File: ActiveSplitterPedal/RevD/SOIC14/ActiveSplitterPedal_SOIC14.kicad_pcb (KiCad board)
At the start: 2 copper layers, 112.5 x 86.4 mm, 97 parts, among them J1 MonoJack2Switch, J2 Barrel_Jack, J3 MonoJack2Switch, J4 MonoJack2Switch, J5 MonoJack2Switch, J6 MonoJack2Switch, U1 AP7370-50SA-7, U11 TL072, U12 TL074, U14 ISA0505, U15 MCP1754S-3302xCB, U16 TC593002ECB, U2 TL072, U3 TL074, U5 TL072, U6 TL074, U8 TL072, U9 TL074

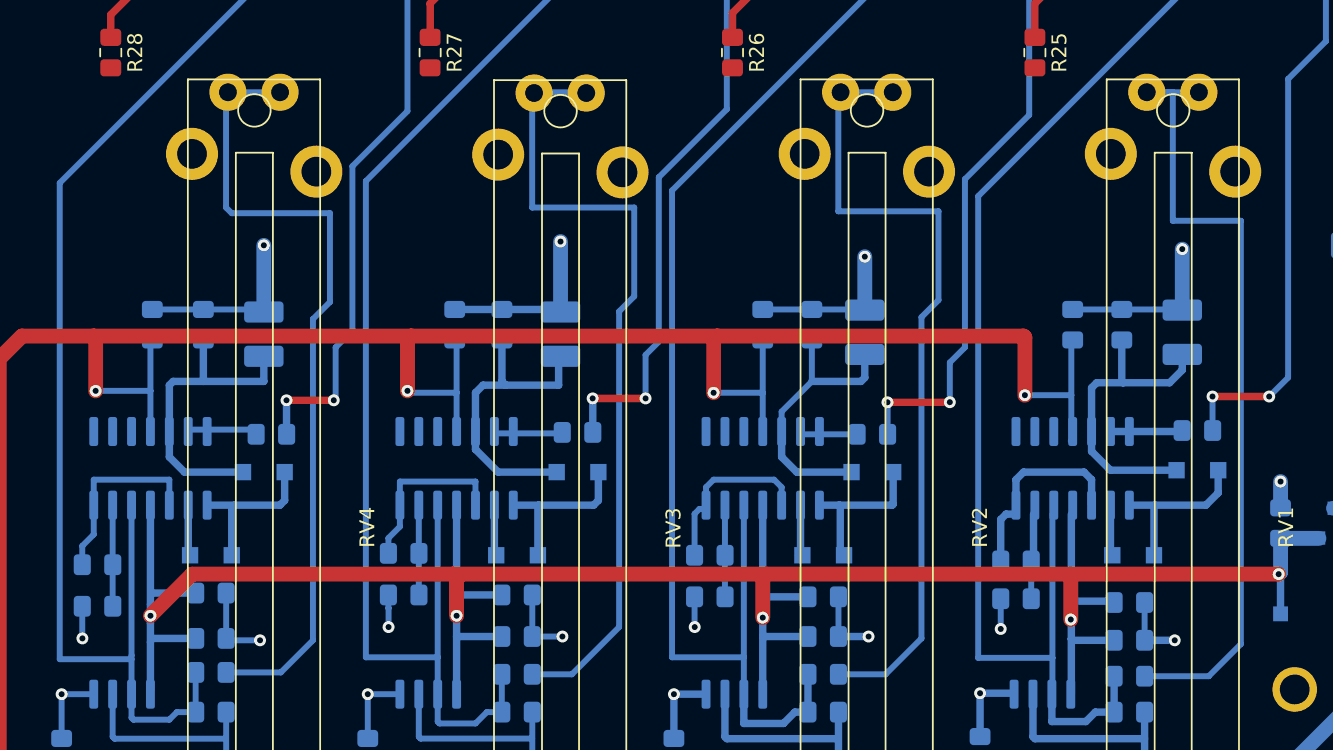
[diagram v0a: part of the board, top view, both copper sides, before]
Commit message: updated hw
added feedback cap to peak detector (help prevent oscillation)
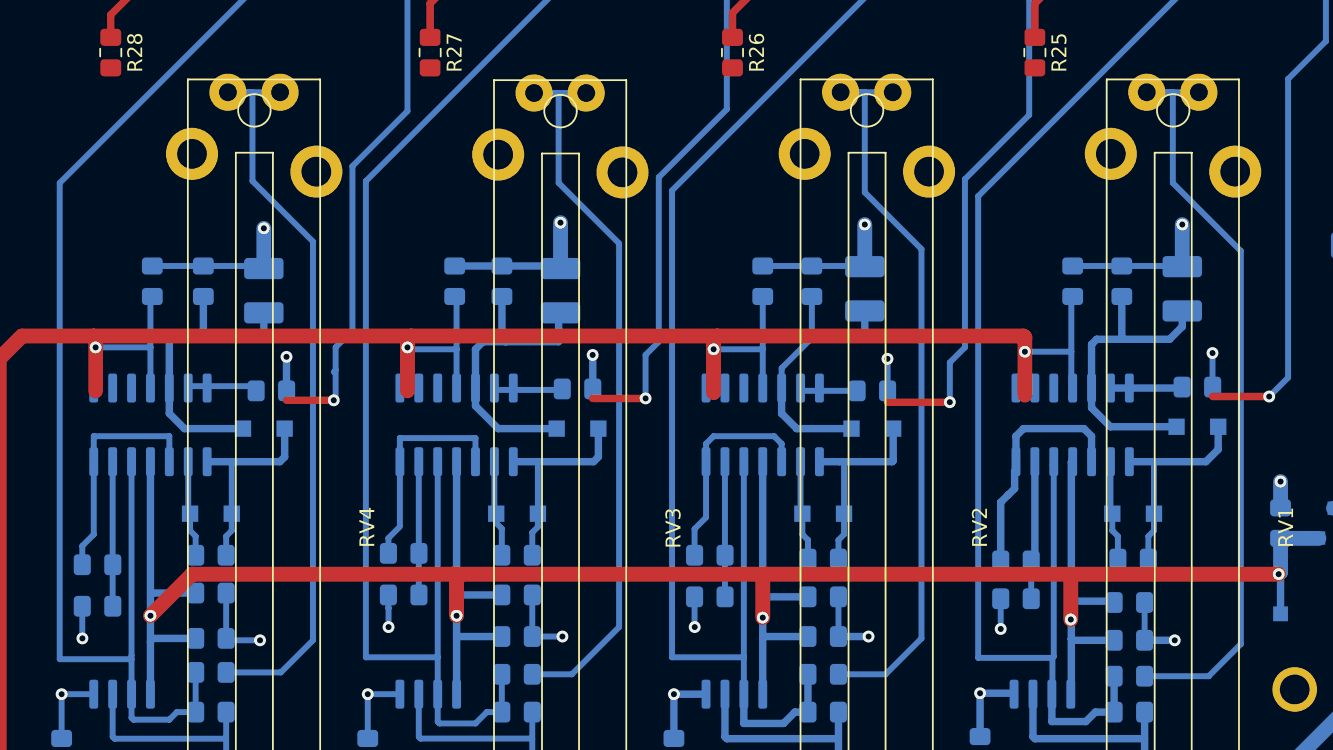
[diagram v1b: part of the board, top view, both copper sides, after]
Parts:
- added C10: 1nF, Capacitor_SMD:C_0805_2012Metric_Pad1.15x1.40mm_HandSolder, B.Cu at (102.4, 100.6)
- added C7: 1nF, Capacitor_SMD:C_0805_2012Metric_Pad1.15x1.40mm_HandSolder, B.Cu at (164.3, 100.8)
- added C8: 1nF, Capacitor_SMD:C_0805_2012Metric_Pad1.15x1.40mm_HandSolder, B.Cu at (143.5, 100.8)
- added C9: 1nF, Capacitor_SMD:C_0805_2012Metric_Pad1.15x1.40mm_HandSolder, B.Cu at (122.9, 100.6)
- moved C16 2.92 mm to (139.4, 82.2)
- moved C27 2.92 mm to (118.7, 82.2)
- moved C38 2.92 mm to (98.4, 82.2)
- moved C5 2.92 mm to (160.3, 82.2)
- moved D1 2.92 mm to (168.7, 91.9)
- moved R10 2.92 mm to (142.7, 82.2)
- moved R16 2.92 mm to (121.9, 82.2)
- moved R21 2.92 mm to (106.4, 89.5)
- moved R22 2.92 mm to (101.9, 82.2)
- moved R4 2.92 mm to (163.6, 82.2)
- moved R9 2.92 mm to (146.8, 89.5)
- moved U12 2.92 mm to (98.3, 91.8)
- moved U3 2.92 mm to (160.3, 91.8)
- moved U6 2.92 mm to (139.4, 91.8)
- moved U9 2.92 mm to (118.9, 91.8)
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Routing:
- net +3V3: track 167.5 -> 180.6 mm
- net VCOM: track 115.6 -> 110.1 mm
- net Net-(R12-Pad2): track 54.0 -> 49.9 mm
- net Net-(R18-Pad2): track 53.9 -> 49.8 mm
- net Net-(R24-Pad2): track 54.4 -> 50.3 mm
- net Net-(R1-Pad2): track 5.75 -> 9.37 mm
- net /sheet5F6AEF15/SIGNAL_INPUT: track 83.9 -> 87.5 mm
- net /PeakDetector1/SIGNAL_INPUT: track 83.3 -> 86.7 mm
- net Net-(R19-Pad2): track 6.16 -> 9.53 mm
- net Net-(C7-Pad1): track 11.2 -> 14.6 mm
- net Net-(C7-Pad2): track 3.42 -> 6.75 mm
- net Net-(C8-Pad1): track 10.0 -> 13.4 mm
- net Net-(C8-Pad2): track 3.42 -> 6.75 mm
- net /sheet5F6A30A3/SIGNAL_INPUT: track 84.0 -> 87.2 mm
- net Net-(R7-Pad2): track 5.91 -> 9.15 mm
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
